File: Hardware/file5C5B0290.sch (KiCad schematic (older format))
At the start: 43 parts, among them J15 Eurorack Connector, J19 Power_Connector, U10 TPS82140, U11 TPS82140, U12 TPSM84209RKHT, U9 TPS82140

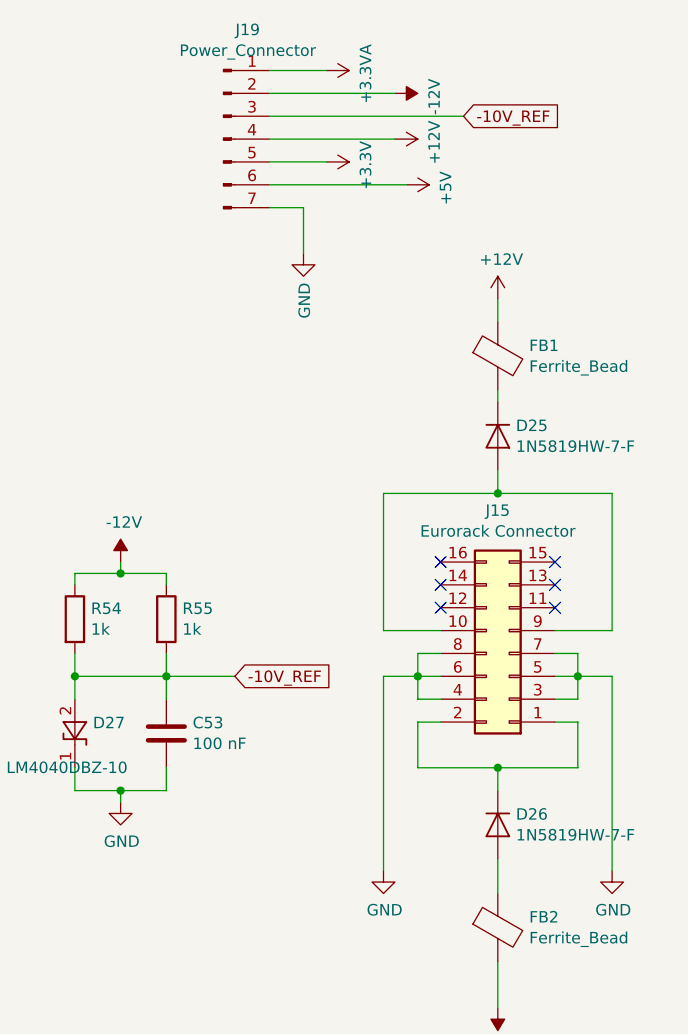
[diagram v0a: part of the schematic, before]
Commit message: Updated to single four layer board
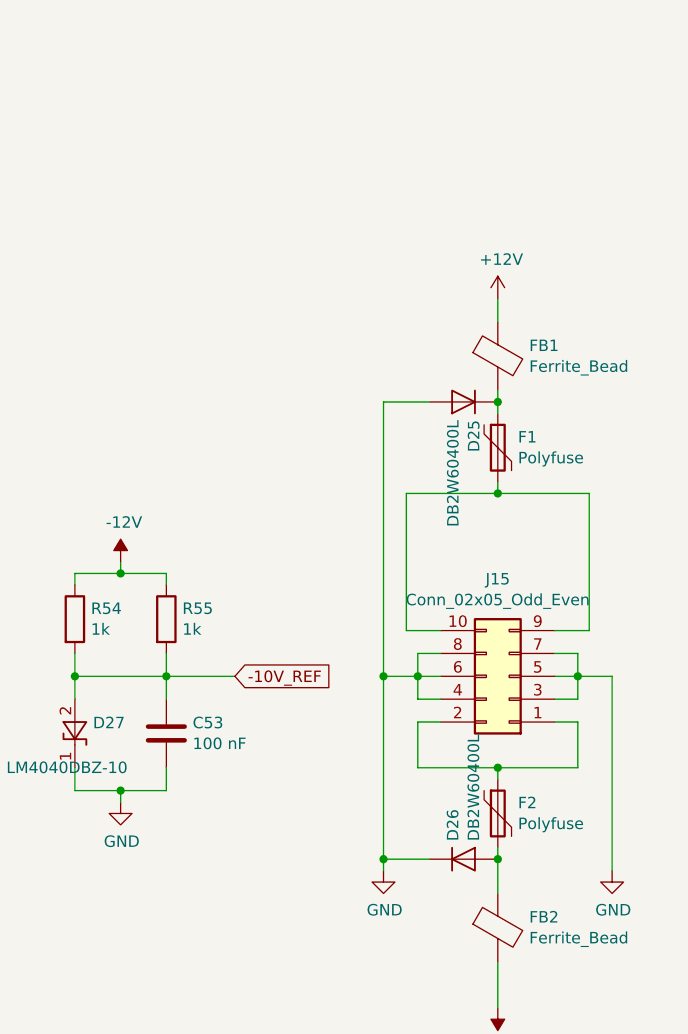
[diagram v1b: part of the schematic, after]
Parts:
- removed J15: Eurorack Connector, Connector_PinHeader_2.54mm:PinHeader_2x08_P2.54mm_Vertical, symbol Connector_Generic:Conn_02x08_Odd_Even
- removed J19: Power_Connector, Connector_PinHeader_2.54mm:PinHeader_1x07_P2.54mm_Vertical, symbol Connector:Conn_01x07_Male
- added F1, F2: Polyfuse, Fuse:Fuse_1812_4532Metric, symbol Device:Polyfuse
- added J15: Conn_02x05_Odd_Even, Connector_IDC:IDC-Header_2x05_P2.54mm_Vertical, symbol Connector_Generic:Conn_02x05_Odd_Even
- D25, D26: value 1N5819HW-7-F -> DB2W60400L; footprint Diode_SMD:D_SOD-123 -> DZ2W:DZ2W160
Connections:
- net GND: now also D25.2 (A), D26.1 (K), J15.3 (Pin_3), J15.4 (Pin_4), J15.5 (Pin_5), J15.6 (Pin_6), J15.7 (Pin_7), J15.8 (Pin_8)
- net at D26.2 (A), FB2.1: now also F2.2
- net at D25.1 (K), FB1.2: now also F1.1
- new net: F1.2, J15.10 (Pin_10), J15.9 (Pin_9)
- new net: F2.1, J15.1 (Pin_1), J15.2 (Pin_2)
- no-connect marks 6 -> 0
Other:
- moved on the sheet: D25, D26
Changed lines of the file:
@@
 	1    0    0    -1
-$EndComp
-$Comp
-L Connector_Generic:Conn_02x08_Odd_Even J15
-U 1 1 5C5B14A9
-P 10350 3600
-F 0 "J15" H 10400 2975 50  0000 C CNN
-F 1 "Eurorack Connector" H 10400 3066 50  0000 C CNN
-F 2 "Connector_PinHeader_2.54mm:PinHeader_2x08_P2.54mm_Vertical" H 10350 3600 50  0001 C CNN
-F 3 "~" H 10350 3600 50  0001 C CNN
-	1    10350 3600
-	-1   0    0    1
 $EndComp
 Wire Wire Line
@@
 	9800 3700 9950 3700
 Wire Wire Line
-	9800 3500 10050 3500
-Wire Wire Line
-	10550 3500 10800 3500
+	9900 3500 10050 3500
+Wire Wire Line
+	10550 3500 10700 3500
 $Comp
 L power:GND #PWR0126
@@
 $EndComp
 Wire Wire Line
-	9800 3700 9800 4550
+	9800 3700 9800 4500
 Wire Wire Line
 	10800 4550 10800 3700
@@
 $EndComp
 Wire Wire Line
-	9800 2900 10300 2900
-Wire Wire Line
-	9800 2900 9800 3500
-Wire Wire Line
-	10800 2900 10800 3500
-Wire Wire Line
-	9950 4100 10300 4100
+	9900 2900 9900 3500
+Wire Wire Line
+	10700 2900 10700 3500
 $Comp
 L Device:D D26
 U 1 1 5C5E8E36
-P 10300 4350
-F 0 "D26" V 10254 4429 50  0000 L CNN
-F 1 "1N5819HW-7-F" V 10345 4429 50  0000 L CNN
-F 2 "Diode_SMD:D_SOD-123" H 10300 4350 50  0001 C CNN
-F 3 "~" H 10300 4350 50  0001 C CNN
-	1    10300 4350
-	0    1    1    0
-$EndComp
-Wire Wire Line
-	10300 4200 10300 4100
-Connection ~ 10300 4100
-Wire Wire Line
-	10300 4100 10650 4100
+P 10150 4500
+F 0 "D26" V 10104 4579 50  0000 L CNN
+F 1 "DB2W60400L" V 10195 4579 50  0000 L CNN
+F 2 "DZ2W:DZ2W160" H 10150 4500 50  0001 C CNN
+F 3 "~" H 10150 4500 50  0001 C CNN
+	1    10150 4500
+	1    0    0    -1
+$EndComp
 $Comp
 L Device:D D25
 U 1 1 5C5EE210
-P 10300 2650
-F 0 "D25" V 10254 2729 50  0000 L CNN
-F 1 "1N5819HW-7-F" V 10345 2729 50  0000 L CNN
-F 2 "Diode_SMD:D_SOD-123" H 10300 2650 50  0001 C CNN
-F 3 "~" H 10300 2650 50  0001 C CNN
-	1    10300 2650
-	0    1    1    0
-$EndComp
-Wire Wire Line
-	10300 2900 10300 2800
-Connection ~ 10300 2900
-Wire Wire Line
-	10300 2900 10800 2900
+P 10150 2500
+F 0 "D25" V 10104 2579 50  0000 L CNN
+F 1 "DB2W60400L" V 10195 2579 50  0000 L CNN
+F 2 "DZ2W:DZ2W160" H 10150 2500 50  0001 C CNN
+F 3 "~" H 10150 2500 50  0001 C CNN
+	1    10150 2500
+	-1   0    0    1
+$EndComp
 $Comp
 L power:+12V #PWR0127
@@
 	1    0    0    -1
 $EndComp
-NoConn ~ 10050 3200
-NoConn ~ 10050 3300
-NoConn ~ 10050 3400
-NoConn ~ 10550 3200
-NoConn ~ 10550 3300
-NoConn ~ 10550 3400
-$Comp
-L power:+3.3VA #PWR0151
-U 1 1 5BE74887
-P 9550 1050
-F 0 "#PWR0151" H 9550 900 50  0001 C CNN
-F 1 "+3.3VA" H 9565 1223 50  0000 C CNN
-F 2 "" H 9550 1050 50  0001 C CNN
-F 3 "" H 9550 1050 50  0001 C CNN
-	1    9550 1050
-	0    1    1    0
-$EndComp
-$Comp
-L power:+12V #PWR0157
-U 1 1 5BE748EC
-P 9850 1350
-F 0 "#PWR0157" H 9850 1200 50  0001 C CNN
-F 1 "+12V" H 9865 1523 50  0000 C CNN
-F 2 "" H 9850 1350 50  0001 C CNN
-F 3 "" H 9850 1350 50  0001 C CNN
-	1    9850 1350
-	0    1    1    0
-$EndComp
-$Comp
-L power:-12V #PWR0159
-U 1 1 5BE749C9
-P 9850 1150
-F 0 "#PWR0159" H 9850 1250 50  0001 C CNN
-F 1 "-12V" H 9865 1323 50  0000 C CNN
-F 2 "" H 9850 1150 50  0001 C CNN
-F 3 "" H 9850 1150 50  0001 C CNN
-	1    9850 1150
-	0    1    1    0
-$EndComp
-Wire Wire Line
-	9300 1050 9550 1050
-Wire Wire Line
-	9300 1150 9850 1150
-Wire Wire Line
-	9300 1350 9850 1350
-$Comp
-L power:GND #PWR0160
-U 1 1 5BE84728
-P 9450 1850
-F 0 "#PWR0160" H 9450 1600 50  0001 C CNN
-F 1 "GND" V 9455 1722 50  0000 R CNN
-F 2 "" H 9450 1850 50  0001 C CNN
-F 3 "" H 9450 1850 50  0001 C CNN
-	1    9450 1850
-	1    0    0    -1
-$EndComp
-Text GLabel 10150 1250 2    50   Input ~ 0
--10V_REF
-Wire Wire Line
-	10150 1250 9300 1250
-$Comp
-L power:+3.3V #PWR0161
-U 1 1 5BE74822
-P 9550 1450
-F 0 "#PWR0161" H 9550 1300 50  0001 C CNN
-F 1 "+3.3V" H 9565 1623 50  0000 C CNN
-F 2 "" H 9550 1450 50  0001 C CNN
-F 3 "" H 9550 1450 50  0001 C CNN
-	1    9550 1450
-	0    1    1    0
-$EndComp
-Wire Wire Line
-	9300 1450 9550 1450
-$Comp
-L Connector:Conn_01x07_Male J19
-U 1 1 5C233DAA
-P 9100 1350
-F 0 "J19" H 9206 1828 50  0000 C CNN
-F 1 "Power_Connector" H 9206 1737 50  0000 C CNN
-F 2 "Connector_PinHeader_2.54mm:PinHeader_1x07_P2.54mm_Vertical" H 9100 1350 50  0001 C CNN
-F 3 "~" H 9100 1350 50  0001 C CNN
-	1    9100 1350
-	1    0    0    -1
-$EndComp
-Wire Wire Line
-	9450 1850 9450 1650
-Wire Wire Line
-	9450 1650 9300 1650
-$Comp
-L power:+5V #PWR0162
-U 1 1 5C23C2BC
-P 9900 1550
-F 0 "#PWR0162" H 9900 1400 50  0001 C CNN
-F 1 "+5V" H 9915 1723 50  0000 C CNN
-F 2 "" H 9900 1550 50  0001 C CNN
-F 3 "" H 9900 1550 50  0001 C CNN
-	1    9900 1550
-	0    1    1    0
-$EndComp
-Wire Wire Line
-	9900 1550 9300 1550
 $Comp
 L Regulator_Switching:TPS82140 U9
@@
 Wire Wire Line
 	10300 4950 10300 5150
+Wire Wire Line
+	10000 4500 9800 4500
+Connection ~ 9800 4500
+Wire Wire Line
+	9800 4500 9800 4550
+Wire Wire Line
+	10000 2500 9800 2500
+Wire Wire Line
+	9800 2500 9800 3700
+Connection ~ 9800 3700
+Wire Wire Line
+	9900 2900 10300 2900
+Wire Wire Line
+	9950 4100 10300 4100
+$Comp
+L Device:Polyfuse F1
+U 1 1 5CADD2FA
+P 10300 2700
+F 0 "F1" H 10388 2746 50  0000 L CNN
+F 1 "Polyfuse" H 10388 2655 50  0000 L CNN
+F 2 "Fuse:Fuse_1812_4532Metric" H 10350 2500 50  0001 L CNN
+F 3 "0ZCG0050FF2C" H 10300 2700 50  0001 C CNN
+	1    10300 2700
+	1    0    0    -1
+$EndComp
+Wire Wire Line
+	10300 2850 10300 2900
+Connection ~ 10300 2900
+Wire Wire Line
+	10300 2900 10700 2900
+Wire Wire Line
+	10300 2550 10300 2500
+Connection ~ 10300 2500
+$Comp
+L Device:Polyfuse F2
+U 1 1 5CAF138F
+P 10300 4300
+F 0 "F2" H 10388 4346 50  0000 L CNN
+F 1 "Polyfuse" H 10388 4255 50  0000 L CNN
+F 2 "Fuse:Fuse_1812_4532Metric" H 10350 4100 50  0001 L CNN
+F 3 "0ZCG0050FF2C" H 10300 4300 50  0001 C CNN
+	1    10300 4300
+	1    0    0    -1
+$EndComp
+Wire Wire Line
+	10300 4500 10300 4450
+Connection ~ 10300 4500
+Wire Wire Line
+	10300 4150 10300 4100
+Connection ~ 10300 4100
+Wire Wire Line
+	10300 4100 10650 4100
+$Comp
+L Connector_Generic:Conn_02x05_Odd_Even J15
+U 1 1 5CBC0E0B
+P 10350 3700
+F 0 "J15" H 10400 3275 50  0000 C CNN
+F 1 "Conn_02x05_Odd_Even" H 10400 3366 50  0000 C CNN
+F 2 "Connector_IDC:IDC-Header_2x05_P2.54mm_Vertical" H 10350 3700 50  0001 C CNN
+F 3 "~" H 10350 3700 50  0001 C CNN
+	1    10350 3700
+	-1   0    0    1
+$EndComp
 $EndSCHEMATC

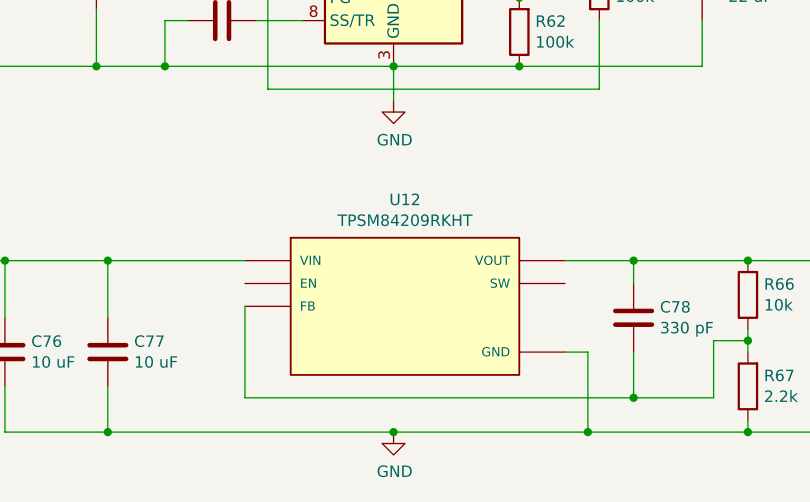
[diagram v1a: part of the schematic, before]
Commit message: Finalized 4 layer design, fixed bad opamp circuits
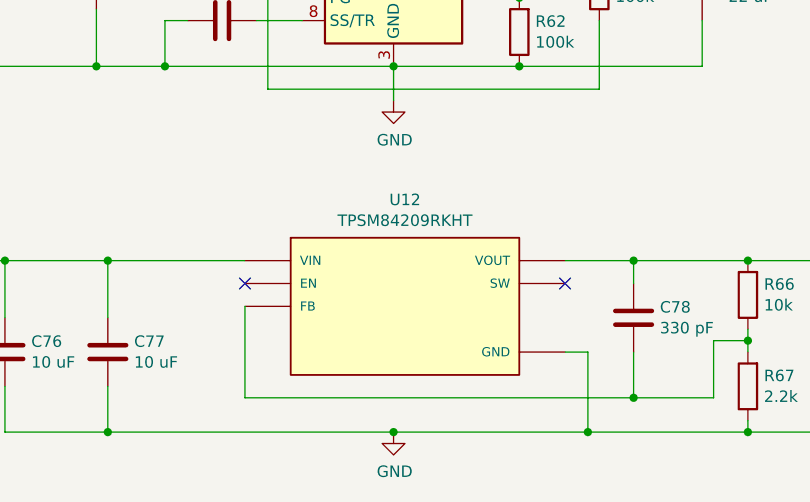
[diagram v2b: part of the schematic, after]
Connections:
- no-connect marks 0 -> 2
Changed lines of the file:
@@
 	-1   0    0    1
 $EndComp
+NoConn ~ 5150 5800
+NoConn ~ 3750 5800
 $EndSCHEMATC

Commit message: Started state machine
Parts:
- removed C76, C77: 10 uF, Capacitor_SMD:C_0603_1608Metric, symbol Device:C
- removed C78: 330 pF, Capacitor_SMD:C_0603_1608Metric, symbol Device:C
- removed C79: 100 uF, Capacitor_SMD:C_0603_1608Metric, symbol Device:C
- removed R66: 10k, Resistor_SMD:R_0603_1608Metric, symbol Device:R
- removed R67: 2.2k, Resistor_SMD:R_0603_1608Metric, symbol Device:R
- removed U12: TPSM84209RKHT, TPSM84209RKHT:VREG_TPSM84209RKHT, symbol TPSM84209RKHT:TPSM84209RKHT
- added C?: 10 uF, Capacitor_SMD:C_0603_1608Metric, symbol Device:C
- added C?: 2.2 nF, Capacitor_SMD:C_0603_1608Metric, symbol Device:C
- added C?: 47 uF, Capacitor_SMD:C_0603_1608Metric, symbol Device:C
- added L?: 1.5 uH, symbol Device:L
- added R? (x2): 100k, Resistor_SMD:R_0603_1608Metric, symbol Device:R
- added R?: 1.18M, Resistor_SMD:R_0603_1608Metric, symbol Device:R
- added U?: TPS621361, symbol Regulator_Switching:TPS621361
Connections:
- net +12V: now also C?.1, U?.1 (VIN), U?.8 (EN)
- net +9V: now also C?.1, L?.2, R?.2, R?.2, U?.6 (VOS)
- net GND: now also C?.2, C?.2, C?.2, R?.1, U?.10 (MODE), U?.11 (VSEL), U?.3 (GND), U?.4 (FB2)
- new net: L?.1, U?.2 (SW)
- new net: R?.1, R?.2, U?.5 (FB)
- new net: R?.1, U?.7 (PG)
- new net: C?.1, U?.9 (SS_TR)
- no-connect marks 2 -> 0
